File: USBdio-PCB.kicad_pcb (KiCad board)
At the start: 2 copper layers, 67 parts, among them P1 TE_RELAY_(ORWH-SH-112D), P2 TE_RELAY_(ORWH-SH-112D), P3 TE_RELAY_(ORWH-SH-112D), P4 TE_RELAY_(ORWH-SH-112D), P5 TE_RELAY_(ORWH-SH-112D), P6 TE_RELAY_(ORWH-SH-112D), P7 TE_RELAY_(ORWH-SH-112D), P8 TE_RELAY_(ORWH-SH-112D), Q1 Q_NPN_EBC, Q10 Q_NPN, Q11 Q_NPN, Q12 Q_NPN, Q13 Q_NPN, Q14 Q_NPN, Q15 Q_NPN, Q16 Q_NPN, Q17 Q_NPN, Q2 Q_NPN_EBC, Q3 Q_NPN_EBC, Q4 Q_NPN_EBC, Q5 Q_NPN_EBC, Q6 Q_NPN_EBC, Q7 Q_NPN_EBC, Q8 Q_NPN_EBC, Q9 Q_NPN_EBC, U1 Arduino_Nano

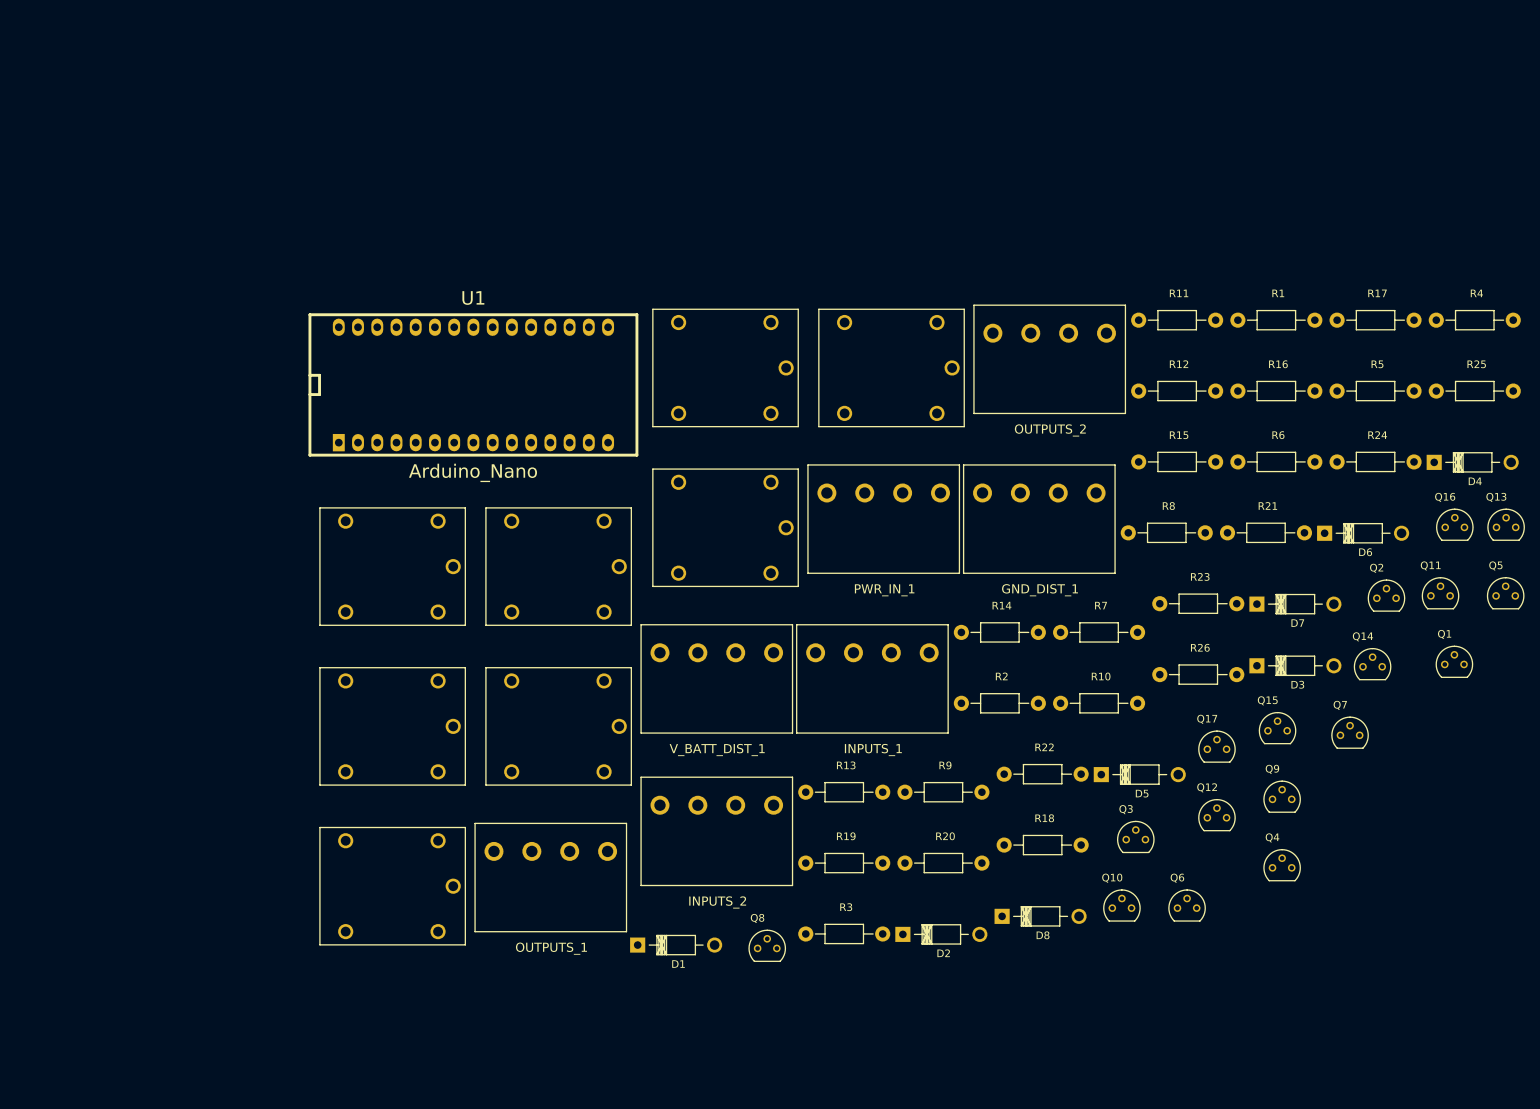
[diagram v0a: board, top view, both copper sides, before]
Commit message: started laying out footprints
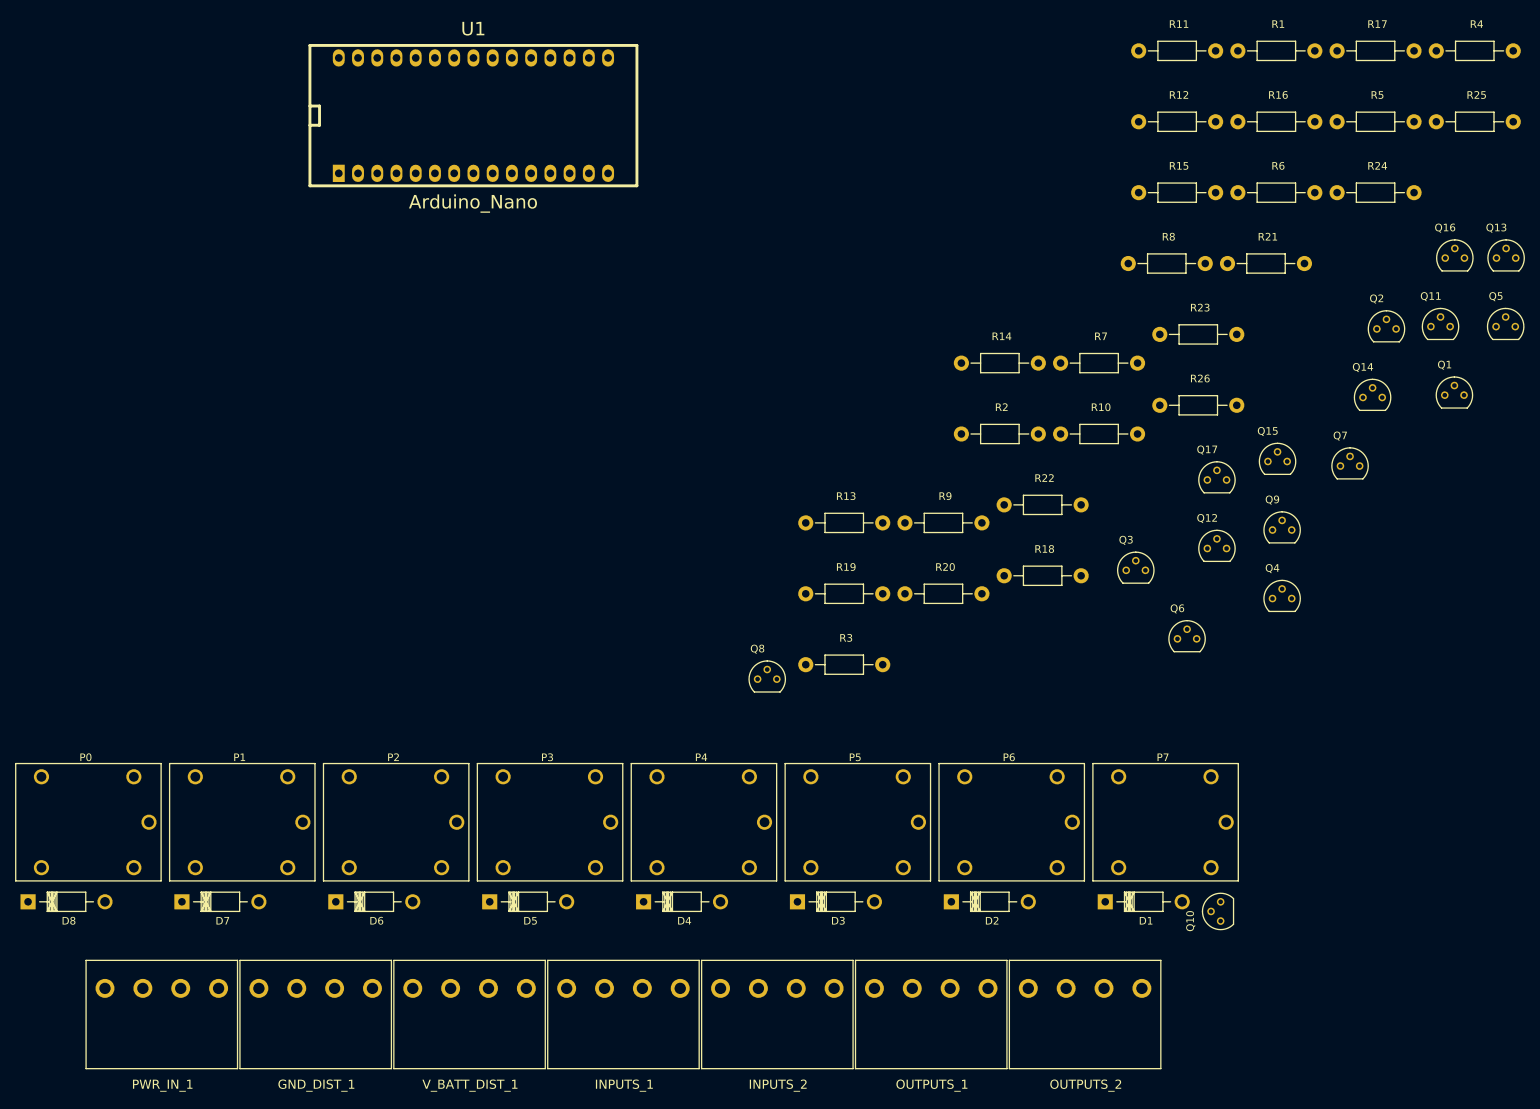
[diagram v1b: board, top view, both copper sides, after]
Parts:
- removed P8: TE_RELAY_(ORWH-SH-112D), USBdio-PCB:TE_RELAY_(ORWH-SH-112D)
- added P0: TE_RELAY_(ORWH-SH-112D), USBdio-PCB:TE_RELAY_(ORWH-SH-112D), F.Cu at (52.1, 115.6)
- moved D7 147.3 mm to (58.4, 132.1)
- moved D6 139.3 mm to (78.7, 132.1)
- moved D8 128.6 mm to (38.1, 132.1)
- moved D4 119.4 mm to (119.4, 132.1)
- moved GND_DIST_1 115.8 mm to (68.6, 143.5)
- moved PWR_IN_1 115.6 mm to (48.3, 143.5)
- moved P1 104.6 mm to (72.4, 115.6)
- moved P7 102.8 mm to (194.3, 115.6)
- moved OUTPUTS_2 86.6 mm to (170.2, 143.5)
- moved D5 82.5 mm to (99.1, 132.1)
- moved P6 68.7 mm to (174.0, 115.6)
- moved D3 68.2 mm to (139.7, 132.1)
- moved D1 62.0 mm to (180.3, 132.1)
- moved INPUTS_1 55.2 mm to (109.2, 143.5)
- moved V_BATT_DIST_1 55.0 mm to (88.9, 143.5)
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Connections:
- P1 pad 2: Net-(D1-Pad2) -> Net-(D7-Pad2)
- P1 pad 4: Net-(OUTPUTS_2-Pad1) -> Net-(OUTPUTS_1-Pad2)
- P2 pad 2: Net-(D2-Pad2) -> Net-(D6-Pad2)
- P2 pad 4: Net-(OUTPUTS_2-Pad2) -> Net-(OUTPUTS_1-Pad3)
- P3 pad 2: Net-(D3-Pad2) -> Net-(D5-Pad2)
- P3 pad 4: Net-(OUTPUTS_2-Pad3) -> Net-(OUTPUTS_1-Pad4)
- P4 pad 4: Net-(OUTPUTS_2-Pad4) -> Net-(OUTPUTS_2-Pad1)
- P5 pad 2: Net-(D5-Pad2) -> Net-(D3-Pad2)
- P5 pad 4: Net-(OUTPUTS_1-Pad1) -> Net-(OUTPUTS_2-Pad2)
- P6 pad 2: Net-(D6-Pad2) -> Net-(D2-Pad2)
- P6 pad 4: Net-(OUTPUTS_1-Pad2) -> Net-(OUTPUTS_2-Pad3)
- P7 pad 2: Net-(D7-Pad2) -> Net-(D1-Pad2)
- P7 pad 4: Net-(OUTPUTS_1-Pad3) -> Net-(OUTPUTS_2-Pad4)

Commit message: finished first rev of PCB
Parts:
- added REF**: MountingHole_2.5mm, Mounting_Holes:MountingHole_2.5mm, F.Cu at (243.8, 66.7)
- added REF**: MountingHole_2.5mm, Mounting_Holes:MountingHole_2.5mm, F.Cu at (243.8, 131.4)
- added REF**: MountingHole_2.5mm, Mounting_Holes:MountingHole_2.5mm, F.Cu at (72.4, 123.8)
- added REF**: MountingHole_2.5mm, Mounting_Holes:MountingHole_2.5mm, F.Cu at (50.2, 81.9)
- moved Q1 175.3 mm to (50.0, 73.7)
- moved R1 152.0 mm to (55.8, 73.7)
- moved R17 140.4 mm to (81.3, 73.7)
- moved R25 128.1 mm to (107.3, 81.9), turned to 180 degrees
- moved Q9 127.2 mm to (75.6, 73.7)
- moved Q16 119.1 mm to (111.1, 81.3)
- moved R2 110.1 mm to (51.3, 66.7)
- moved R16 106.9 mm to (97.8, 66.7)
- moved Q17 103.8 mm to (90.2, 81.3)
- moved R26 102.4 mm to (86.4, 81.9), turned to 180 degrees
- moved Q7 93.9 mm to (117.5, 73.7)
- moved R24 93.4 mm to (128.3, 81.9), turned to 180 degrees
- moved R18 92.9 mm to (76.8, 66.7)
- moved R19 92.7 mm to (233.0, 81.9), turned to 180 degrees
- moved U1 92.0 mm to (56.5, 110.9), turned to 90 degrees
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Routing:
- net Net-(D1-Pad1): track 0.00 -> 426.7 mm, vias 0 -> 1
- net Net-(R1-Pad2): track 0.00 -> 336.5 mm, vias 0 -> 1
- net Net-(INPUTS_2-Pad4): track 0.00 -> 261.5 mm
- net Net-(INPUTS_2-Pad3): track 0.00 -> 247.5 mm
- net Net-(INPUTS_2-Pad2): track 0.00 -> 235.1 mm
- net Net-(INPUTS_2-Pad1): track 0.00 -> 222.1 mm
- net Net-(R19-Pad2): track 0.00 -> 216.5 mm, vias 0 -> 1
- net Net-(INPUTS_1-Pad4): track 0.00 -> 210.2 mm
- net Net-(Q2-Pad3): track 0.00 -> 205.8 mm, vias 0 -> 1
- net Net-(INPUTS_1-Pad3): track 0.00 -> 196.7 mm
- net Net-(R20-Pad2): track 0.00 -> 193.8 mm, vias 0 -> 1
- net Net-(INPUTS_1-Pad2): track 0.00 -> 182.7 mm
- net Net-(Q3-Pad3): track 0.00 -> 182.7 mm, vias 0 -> 1
- net Net-(R21-Pad2): track 0.00 -> 170.5 mm, vias 0 -> 1
- net Net-(INPUTS_1-Pad1): track 0.00 -> 167.1 mm
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- added copper zone on B.Cu, net GND
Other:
- board outline added: 201.3 x 72.4 mm
- net class 5 Amps added: clearance 0.2, trace_width 2, via_dia 0.6, via_drill 0.4
- net class High Amps added: clearance 0.4, trace_width 4.5, via_dia 0.6, via_drill 0.4

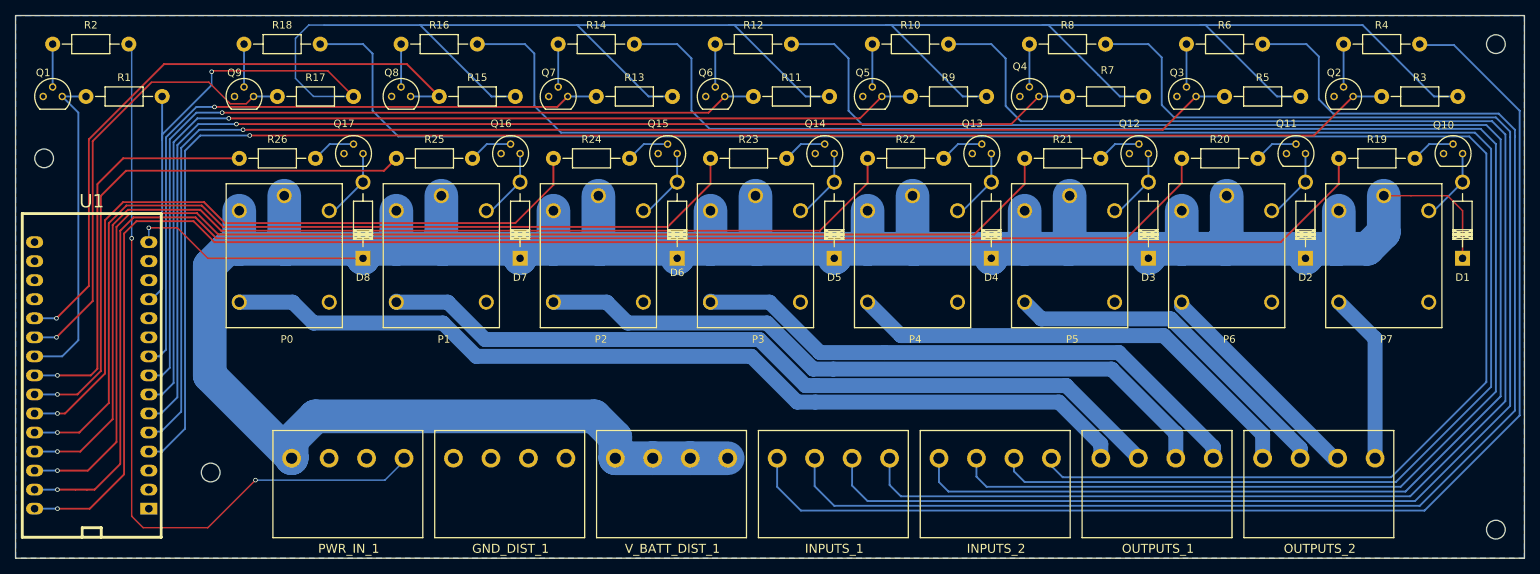
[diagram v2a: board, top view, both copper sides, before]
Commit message: created CircuitCAM and LMD files
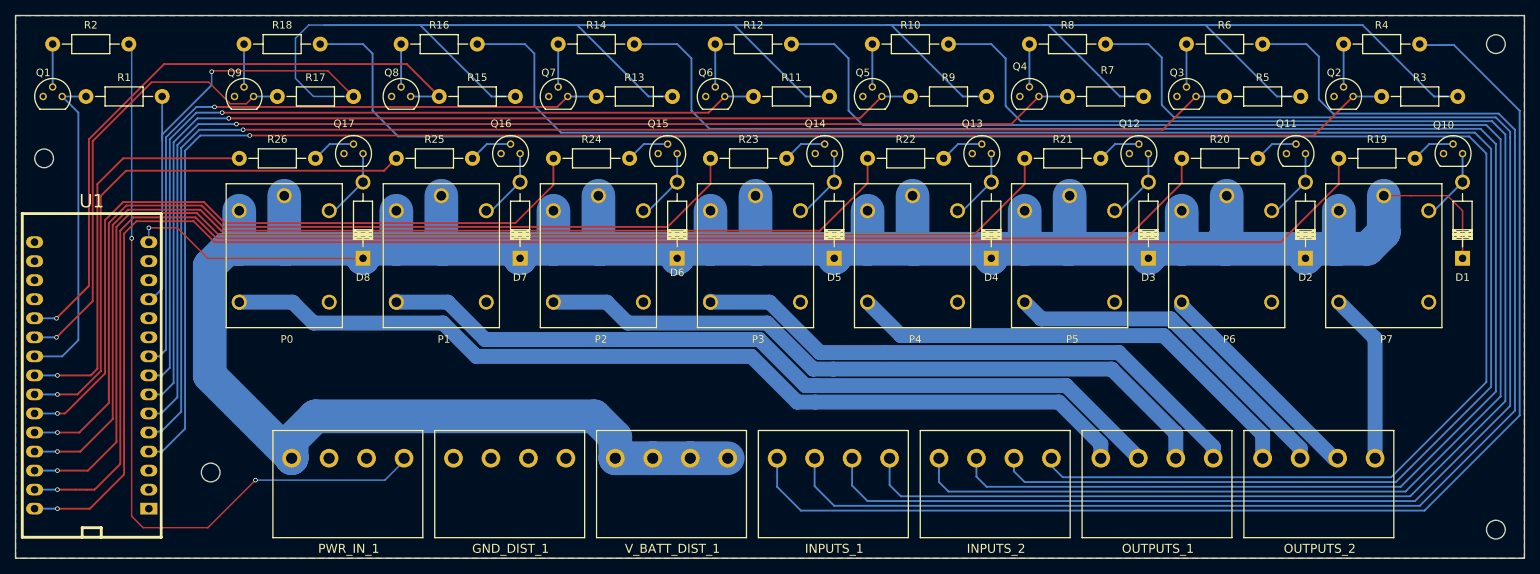
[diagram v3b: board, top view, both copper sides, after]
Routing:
- added copper zone on F.Cu, net GND
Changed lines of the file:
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@@
-(kicad_pcb (version 4) (host pcbnew 4.0.3+e1-6302~38~ubuntu16.04.1-stable)
+(kicad_pcb (version 4) (host pcbnew 4.0.2-stable)
   (general
     (links 138)
     (no_connects 0)
-    (area 41.836429 62 252.168572 136.22)
+    (area 41.761429 61.85 252.243572 136.12)
     (thickness 1.6)
     (drawings 4)
@@
     (pad_to_mask_clearance 0.2)
     (aux_axis_origin 0 0)
-    (visible_elements FFFEFF7F)
+    (visible_elements 7FFDFF7F)
     (pcbplotparams
       (layerselection 0x00030_80000001)
@@
       (outputformat 1)
       (mirror false)
-      (drillshape 1)
+      (drillshape 0)
       (scaleselection 1)
       (outputdirectory ""))
@@
     (connect_pads (clearance 0.508))
     (min_thickness 0.254)
+    (fill yes (arc_segments 16) (thermal_gap 0.508) (thermal_bridge_width 1))
+    (polygon
+      (pts
+        (xy 247.65 62.865) (xy 247.65 135.255) (xy 46.355 135.255) (xy 46.355 62.865)
+      )
+    )
+  )
+  (zone (net 1) (net_name GND) (layer F.Cu) (hatch edge 0.508)
+    (connect_pads (clearance 0.508))
+    (min_thickness 0.254)

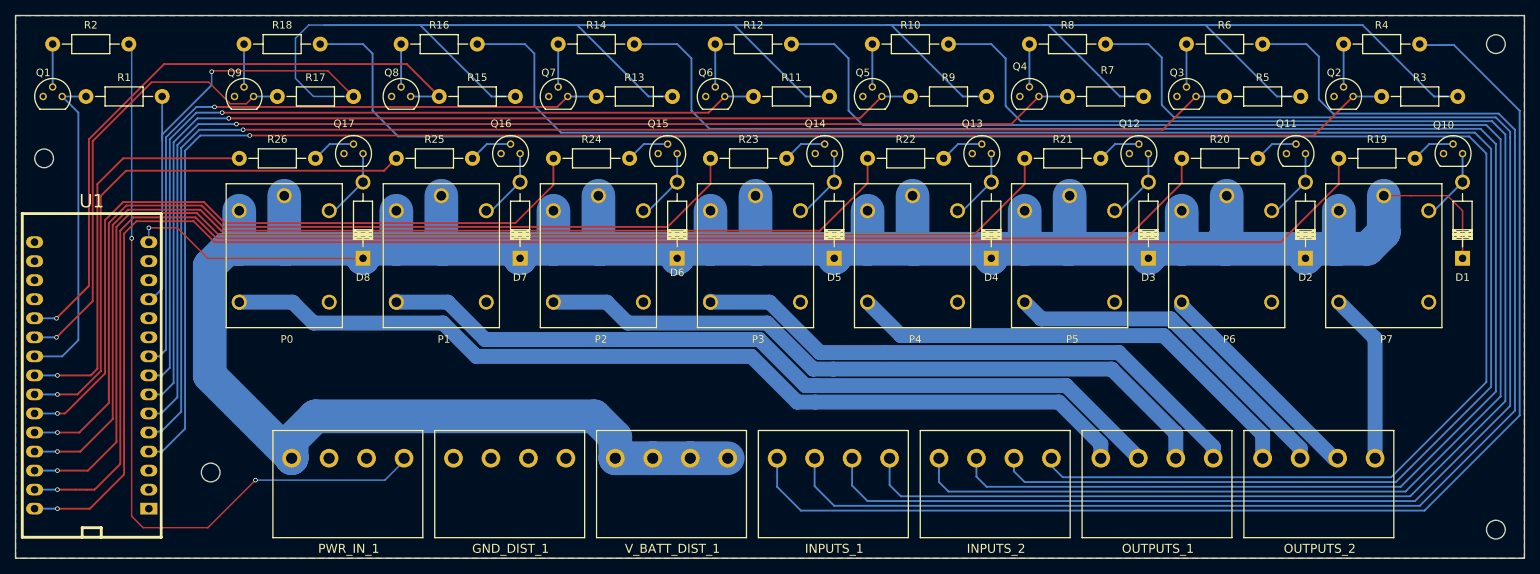
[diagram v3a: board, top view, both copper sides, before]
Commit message: bigger pads for transistors and vias
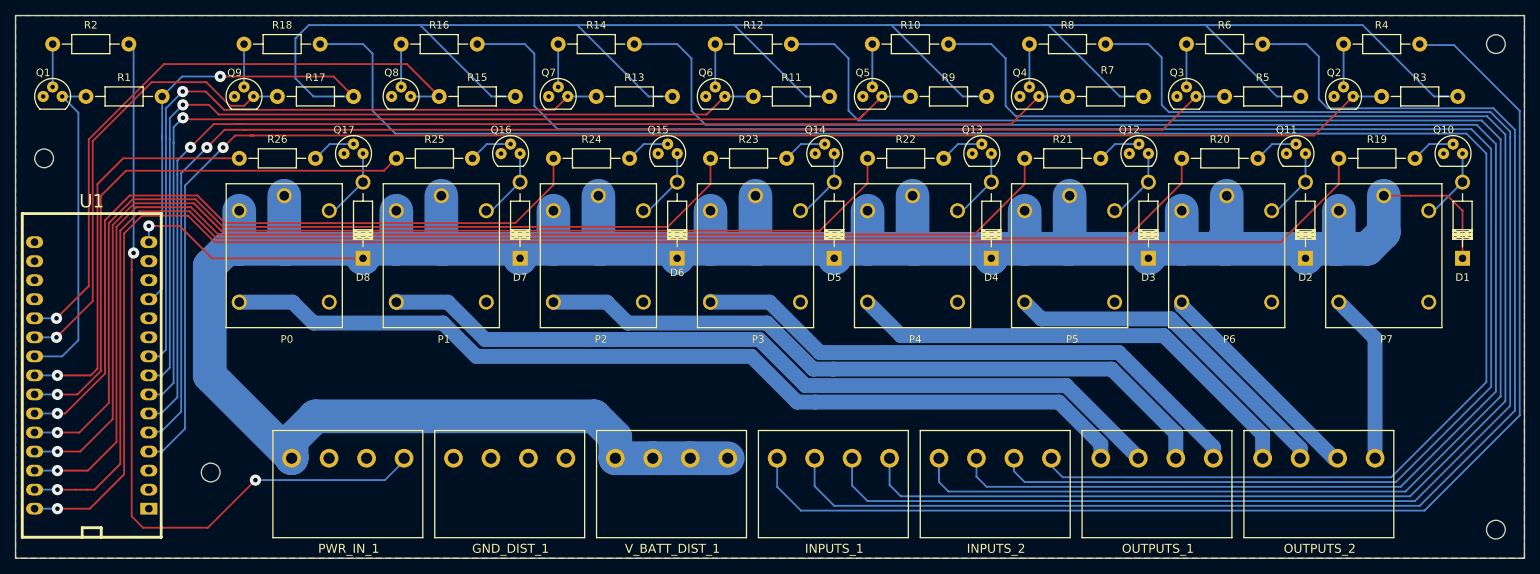
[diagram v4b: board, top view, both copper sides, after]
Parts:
- Q1, Q10, Q11, Q12, Q13, Q14, Q15, Q16, Q17, Q2, Q3, Q4, Q5, Q6, Q7, Q8, Q9: footprint TO_SOT_Packages_THT:TO-92_Molded_Narrow -> USBdio-PCB:TO-92_big_pads
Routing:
- net Net-(Q7-Pad3): track 90.6 -> 94.9 mm
- net Net-(R1-Pad2): track 336.5 -> 332.8 mm
- net Net-(Q6-Pad3): track 113.9 -> 116.7 mm
- net Net-(Q5-Pad3): track 136.9 -> 139.2 mm
- net Net-(Q2-Pad3): track 205.8 -> 203.6 mm
- net Net-(Q3-Pad3): track 182.7 -> 181.2 mm
- net Net-(R24-Pad2): track 99.7 -> 100.4 mm
- net Net-(R22-Pad2): track 146.8 -> 147.5 mm
- net Net-(R23-Pad2): track 123.8 -> 124.4 mm
- net Net-(R20-Pad2): track 193.8 -> 194.5 mm
- net Net-(R21-Pad2): track 170.5 -> 171.2 mm
- net Net-(R19-Pad2): track 216.5 -> 217.1 mm
- net Net-(PWR_IN_1-Pad4): track 104.2 -> 104.7 mm
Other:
- net class 5 Amps: via_dia 0.6 -> 1.5; via_drill 0.4 -> 0.6
- net class Default: via_dia 0.6 -> 1.5; via_drill 0.4 -> 0.6
- net class High Amps: via_dia 0.6 -> 1.5; via_drill 0.4 -> 0.6
